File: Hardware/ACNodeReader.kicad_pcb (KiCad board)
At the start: 2 copper layers, 50 x 50 mm, 28 parts, among them J1 8P8C, J2 AVR-ISP-6, J3 Conn_01x04_Female, J5 Conn_01x04_Female, SW2 SW_Push, U1 L78L05_SOT89, U2 ATmega88PB-AU, U3 ISL8489EIBZ, U4 SI7060-B-00-IV, Y1 Crystal_GND24

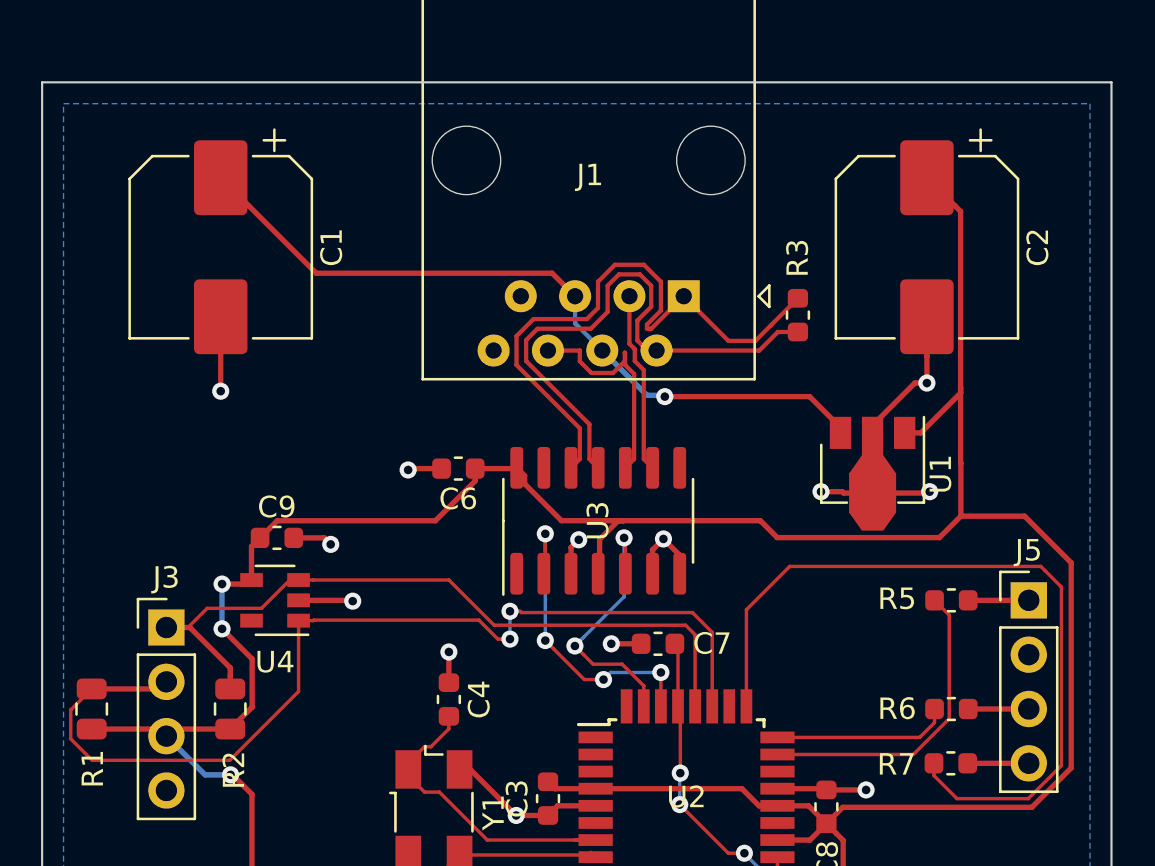
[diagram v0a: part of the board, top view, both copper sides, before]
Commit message: Toying with the circuit a bit
Removed the capacitor across reset since it breaks DebugWire which
is worth having usable because it helps when all hell breaks loose :-)

Added zero ohm links for switching LED from common anode to common cathode

Switched capacitors to (much smaller) MLCC variants in preparation for attempting
to cram everything into a smaller board
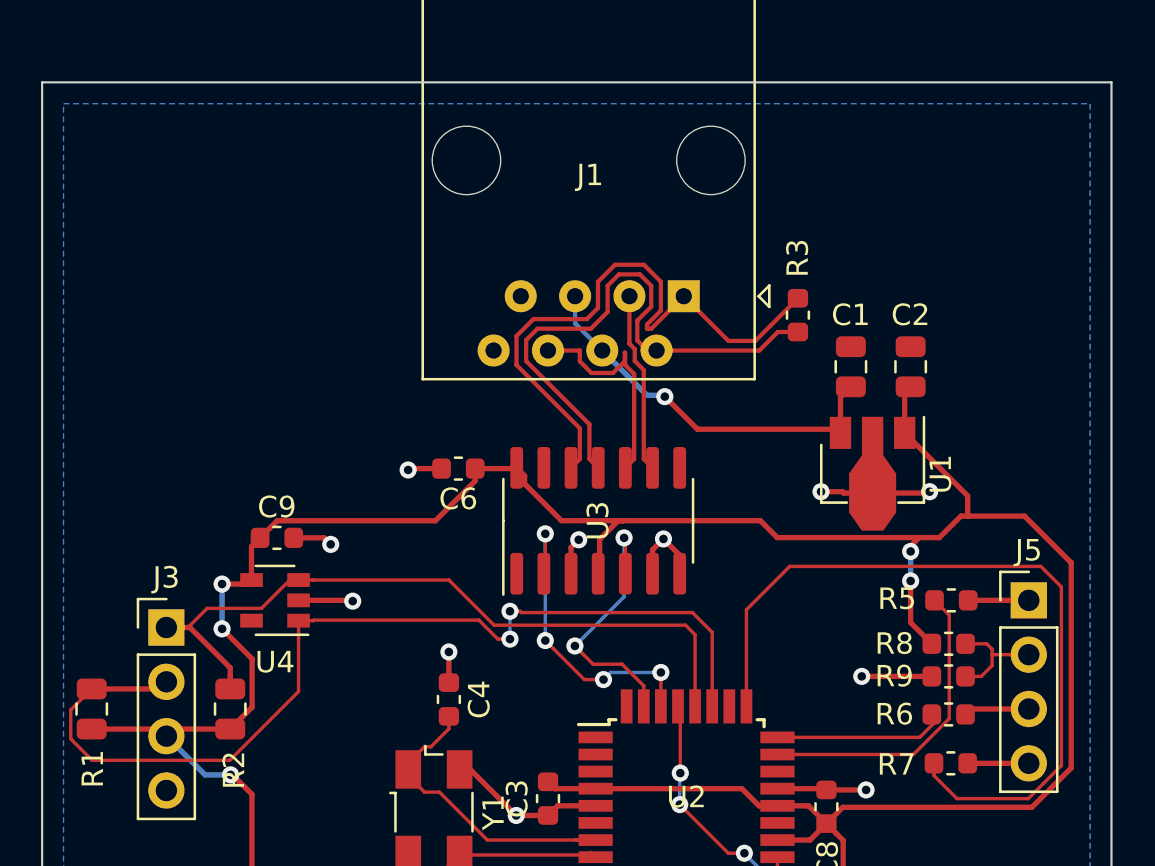
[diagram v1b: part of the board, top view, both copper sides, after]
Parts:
- removed C7: 4.7nF, Capacitor_SMD:C_0603_1608Metric
- added R8: DNF, Resistor_SMD:R_0603_1608Metric, F.Cu at (167.4, 111.3)
- added R9: 0R, Resistor_SMD:R_0603_1608Metric, F.Cu at (167.4, 112.8)
- C1, C2: value 470u -> 10u; footprint Capacitor_SMD:CP_Elec_8x10 -> Capacitor_SMD:C_0805_2012Metric
- moved C1 30.0 mm to (162.8, 98.3), turned to 90 degrees
- moved C2 5.64 mm to (165.6, 98.3), turned to 90 degrees
- moved R6 0.28 mm to (167.4, 114.6)
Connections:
- J5 pad 2: GND -> Net-(J5-Pad2)
- U2 pad 1: (no net) -> Net-(U2-Pad1)
- U2 pad 10: (no net) -> Net-(U2-Pad10)
- U2 pad 12: (no net) -> Net-(U2-Pad12)
- U2 pad 13: (no net) -> Net-(U2-Pad13)
- U2 pad 14: (no net) -> Net-(U2-Pad14)
- U2 pad 19: (no net) -> Net-(U2-Pad19)
- U2 pad 2: (no net) -> Net-(U2-Pad2)
- U2 pad 22: (no net) -> Net-(U2-Pad22)
- U2 pad 26: (no net) -> Net-(U2-Pad26)
- U2 pad 3: (no net) -> Net-(U2-Pad3)
- U2 pad 32: (no net) -> Net-(U2-Pad32)
- U2 pad 6: (no net) -> Net-(U2-Pad6)
- U2 pad 9: (no net) -> Net-(U2-Pad9)
- U4 pad 5: (no net) -> Net-(U4-Pad5)
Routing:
- net +12V: track 34.8 -> 18.4 mm
- net GND: track 55.6 -> 47.1 mm, vias 15 -> 13
- net +5V: track 155.4 -> 148.7 mm, vias 3 -> 5
- net Net-(J5-Pad2): track 0.00 -> 5.28 mm
- net Net-(J2-Pad5): track 24.6 -> 21.6 mm

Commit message: New, smaller, better PCB design
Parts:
- removed SW2: SW_Push, Button_Switch_THT:SW_PUSH_6mm
- added D1: D_Zener, Diode_SMD:D_SOD-323F, F.Cu at (116.6, 98.7)
- added H1: MountingHole, MountingHole:MountingHole_3.2mm_M3_DIN965, F.Cu at (117.5, 67.5)
- added H2: MountingHole, MountingHole:MountingHole_3.2mm_M3_DIN965, F.Cu at (142.8, 95.2)
- added J4: Conn_01x02_Male, Connector_PinHeader_2.54mm:PinHeader_1x02_P2.54mm_Horizontal, F.Cu at (145.7, 86.4)
- added J6: Conn_01x04_Male, Connector_PinHeader_2.54mm:PinHeader_1x04_P2.54mm_Horizontal, B.Cu at (114.1, 77.6)
- added J7: Conn_01x04_Male, Connector_PinHeader_2.54mm:PinHeader_1x04_P2.54mm_Vertical, F.Cu at (112.5, 66.0)
- J1: value 8P8C -> Conn_01x08_Male; footprint Connector_RJ:RJ45_Amphenol_54602-x08_Horizontal -> Connector_PinHeader_2.54mm:PinHeader_1x08_P2.54mm_Horizontal
- J2: footprint Tag-Connect:TC2030-MCP -> Tag-Connect:TC2030-MCP-NL
- J5: footprint Connector_PinHeader_2.54mm:PinHeader_1x04_P2.54mm_Vertical -> Connector_PinHeader_2.54mm:PinHeader_1x04_P2.54mm_Horizontal
- R1, R2, R4: footprint Resistor_SMD:R_0805_2012Metric -> Resistor_SMD:R_0603_1608Metric
- U4: value SI7060-B-00-IV -> LM75C; footprint Package_TO_SOT_SMD:SOT-23-5 -> Package_SO:SO-8_3.9x4.9mm_P1.27mm
- Y1: footprint Crystal:Crystal_SMD_Abracon_ABM3B-4Pin_5.0x3.2mm -> Crystal:Crystal_SMD_7050-4Pin_7.0x5.0mm
- moved R4 63.0 mm to (129.0, 72.8), turned to 0 degrees
- moved C8 53.8 mm to (123.8, 80.5), turned to 270 degrees
- moved C4 47.2 mm to (119.0, 73.8), turned to 180 degrees
- moved C5 46.7 mm to (119.2, 84.7), turned to 0 degrees
- moved J2 46.7 mm to (133.5, 91.1), turned to 0 degrees
- moved Y1 46.6 mm to (119.0, 79.3)
- moved R1 45.7 mm to (135.8, 69.4), turned to 0 degrees
- moved U2 45.4 mm to (130.2, 80.5)
- moved J3 44.1 mm to (134.1, 66.5), turned to 270 degrees
- moved R2 43.1 mm to (135.8, 71.2), turned to 0 degrees
- moved R9 43.0 mm to (142.2, 78.0)
- moved R3 42.7 mm to (118.5, 87.2), turned to 0 degrees
- moved R7 41.7 mm to (142.2, 83.6)
- moved C10 41.7 mm to (142.7, 87.4), turned to 270 degrees
- moved J5 41.7 mm to (145.7, 76.2)
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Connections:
- J1 pad 1: /RX+ -> GND
- J1 pad 2: /RX- -> GND
- J1 pad 3: /TX+ -> /TX-
- J1 pad 6: /TX- -> /TX+
- J1 pad 7: GND -> /RX-
- J1 pad 8: GND -> /RX+
- R1 pad 1: i2c_SDA -> i2c_SCL
- R2 pad 1: i2c_SCL -> i2c_SDA
- R5 pad 2: Net-(R5-Pad2) -> /LED1
- R6 pad 2: Net-(R6-Pad2) -> /LED2
- R7 pad 2: Net-(R7-Pad2) -> /LED3
- R8 pad 2: +5V -> GND
- R9 pad 1: GND -> +5V
- U2 pad 10: Net-(U2-Pad10) -> /LED2
- U2 pad 13: Net-(U2-Pad13) -> /LED3
- U2 pad 23: Net-(R5-Pad2) -> Net-(U2-Pad23)
- U2 pad 24: Net-(R6-Pad2) -> Net-(U2-Pad24)
- U2 pad 25: Net-(R7-Pad2) -> Net-(U2-Pad25)
- U2 pad 9: Net-(U2-Pad9) -> /LED1
- U4 pad 2: GND -> i2c_SCL
- U4 pad 3: i2c_SCL -> Net-(U4-Pad3)
- U4 pad 4: +5V -> GND
- U4 pad 5: Net-(U4-Pad5) -> GND
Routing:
- net Net-(R7-Pad2): track 36.5 -> 0.00 mm
- net /uC_TX: track 12.7 -> 42.0 mm
- net /uC_RX: track 14.8 -> 33.7 mm, vias 4 -> 2
- net /LED1: track 0.00 -> 18.7 mm
- net +5V: track 148.7 -> 166.2 mm, vias 5 -> 12
- net /LED2: track 0.00 -> 16.8 mm, vias 0 -> 2
- net GND: track 47.1 -> 62.4 mm, vias 13 -> 12
- net /RX+: track 28.6 -> 13.7 mm
- net Net-(R5-Pad2): track 14.5 -> 0.00 mm
- net /LED3: track 0.00 -> 12.9 mm, vias 0 -> 2
- net /RX-: track 26.5 -> 14.6 mm
- net i2c_SCL: track 34.8 -> 44.2 mm, vias 0 -> 1
- net Net-(C10-Pad1): track 30.3 -> 21.2 mm, vias 0 -> 2
- net Net-(R6-Pad2): track 8.27 -> 0.00 mm
- net Net-(J2-Pad1): track 17.7 -> 9.89 mm
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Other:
- board size 50 x 50 mm -> 40.4 x 42.7 mm
- copper layers 2 -> 4
- net class Power: trace_width 0.25 -> 0.5
- board text added: "+5V"
- board text added: "2020-08-27"
- board text added: "ACNode Reader Board V1.0 Designed by Michael Cullen"
- board text added: "Blue"
- board text added: "Blue/White"
- board text added: "Brown"
- board text added: "Brown/White"
- board text added: "Common"
- board text added: "Display?"
- board text added: "Fit R8 for common anode Fit R9 for common cathode Fit both for exciting times (briefly)"
- board text added: "GND"
- board text added: "Gr/Wh"
- board text added: "Green"
- board text added: "LED"
- board text added: "O/W"
- board text added: "Orange"
- board text added: "PN532 Goes Here"
- board text added: "RX"
- board text added: "Red"
- board text added: "Switch"
- board text added: "TX"
- board text added: "To ACNode"
- board text added: "To ACNode (Alternative)"

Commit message: Added note about reversed pinout
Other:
- board text added: "Connector Labelled Backwards!"

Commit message: Added some notes to schematic and updated firmware with new board support
getting there!
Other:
- board text added: "U4 Label upside down!"

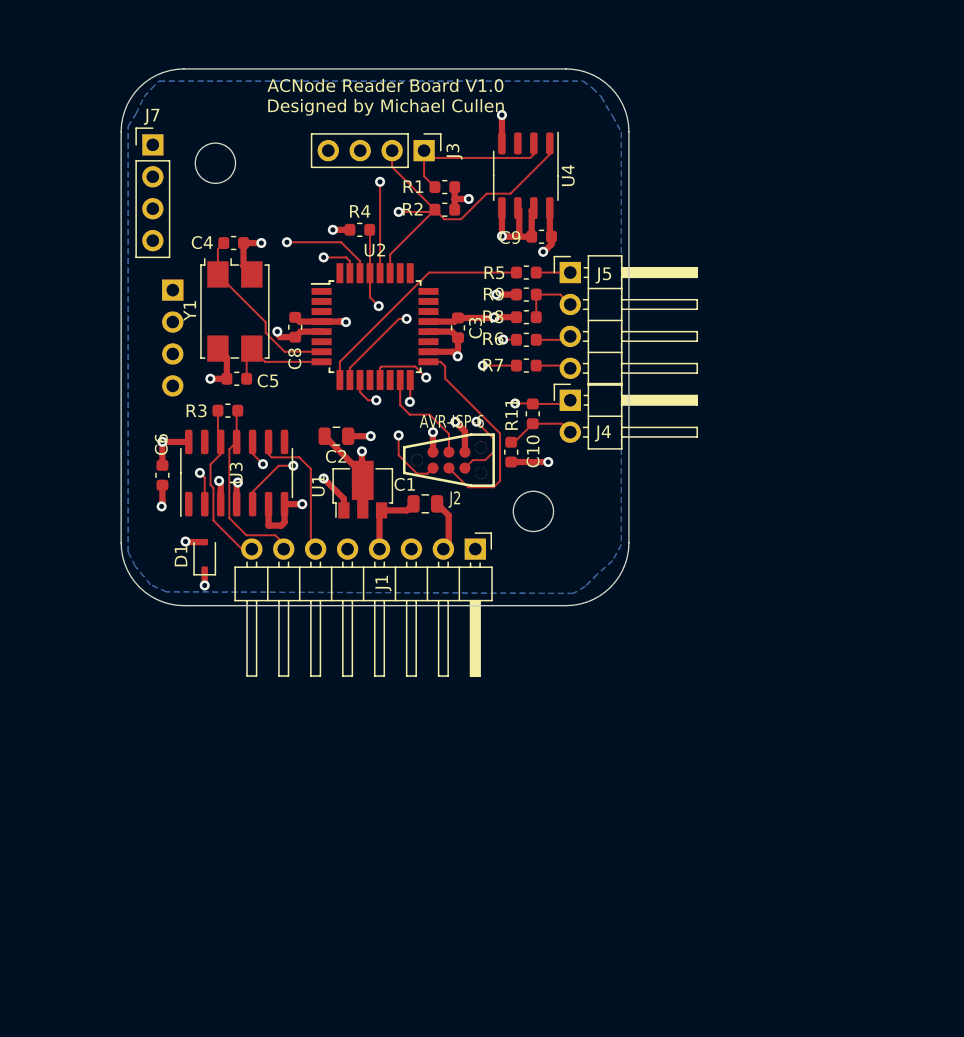
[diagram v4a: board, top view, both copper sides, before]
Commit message: Hardware V1.1 - 3.3V with chunkier 5V regulator
The 1.0 5V regulator wasn't chunky enough, so this board has a larger
one to support the current draw of the PN532 module. Additionally, a
capacitor has been added near to the PN532 module connector to assist in
smoothing the supply to it.

Most of the board now runs at 3.3V, derived from the 5V rail. This is to
support direct connection to an ACNode, which only support 3.3V IO. This
required slowing the AVR down to 12MHz. An alternative option would have
been to use a level shifter on the TX line.
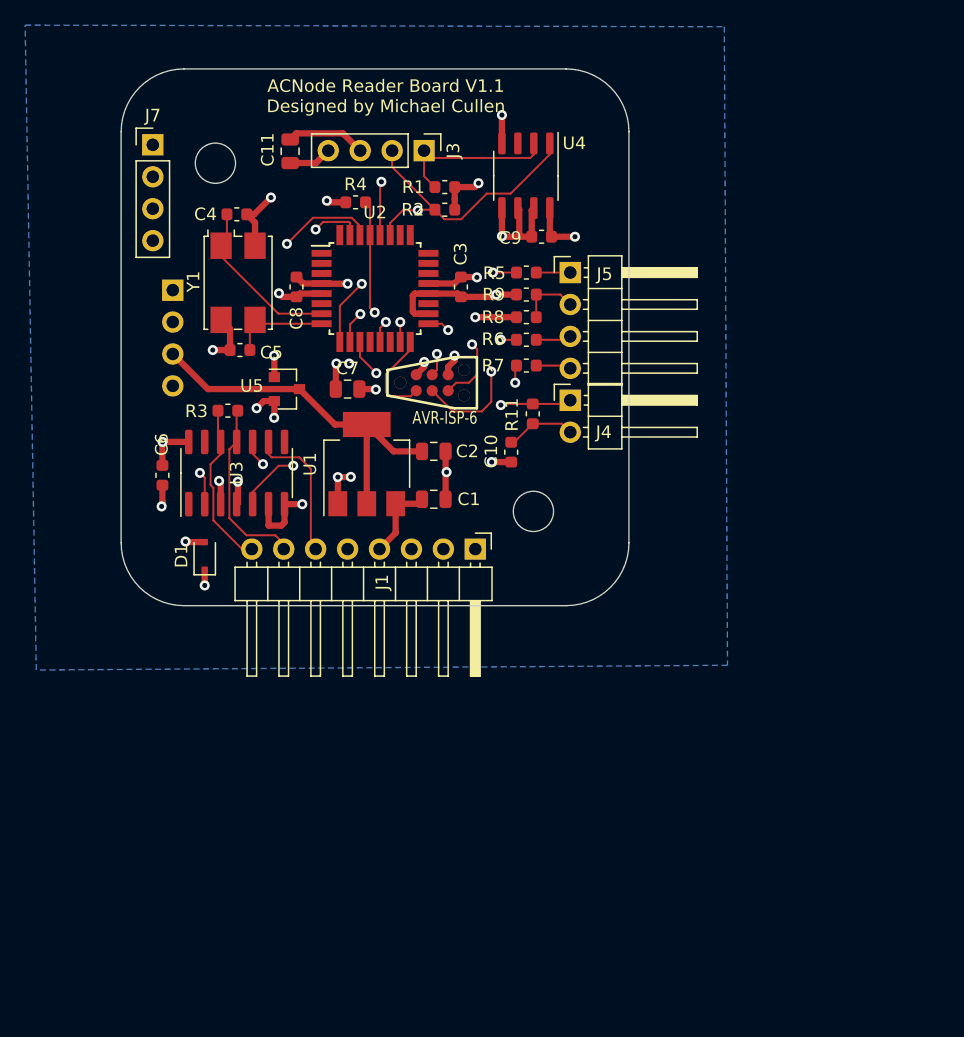
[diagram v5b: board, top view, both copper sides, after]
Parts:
- added C11: 10u, Capacitor_SMD:C_0805_2012Metric, F.Cu at (123.4, 66.5)
- added C7: 10u, Capacitor_SMD:C_0805_2012Metric, F.Cu at (128.0, 85.5)
- added U5: MCP1700-3302E_SOT23, Package_TO_SOT_SMD:SOT-23, F.Cu at (123.2, 85.5)
- U1: value L78L05_SOT89 -> NCP1117-5.0_SOT223; footprint Package_TO_SOT_SMD:SOT-89-3 -> Package_TO_SOT_SMD:SOT-223-3_TabPin2
- U3: value ISL8489EIBZ -> ISL3176EIBZ
- Y1: value Crystal_GND24 -> 12MHz
- moved C2 7.84 mm to (134.9, 90.4), turned to 0 degrees
- moved J2 6.30 mm to (132.2, 85.0)
- moved C3 3.27 mm to (137.0, 77.3)
- moved C8 3.21 mm to (124.0, 77.3)
- moved U2 3.03 mm to (130.2, 77.5)
- moved Y1 2.30 mm to (119.3, 77.0)
- moved C4 2.30 mm to (119.2, 71.6)
- moved C5 2.30 mm to (119.5, 82.4)
- moved R4 2.21 mm to (128.7, 70.6)
- moved U1 2.06 mm to (129.5, 91.4)
- moved C1 0.77 mm to (134.9, 94.2)
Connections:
- C3 pad 2: +5V -> +3V3
- C6 pad 1: +5V -> +3V3
- C8 pad 1: +5V -> +3V3
- C9 pad 1: +5V -> +3V3
- J2 pad 2: +5V -> +3V3
- R1 pad 2: +5V -> +3V3
- R11 pad 2: +5V -> +3V3
- R2 pad 2: +5V -> +3V3
- R4 pad 1: +5V -> +3V3
- R9 pad 1: +5V -> +3V3
- U1 pad 1: +5V -> GND
- U1 pad 2: GND -> +5V
- U2 pad 1: Net-(U2-Pad1) -> (no net)
- U2 pad 12: Net-(U2-Pad12) -> (no net)
- U2 pad 14: Net-(U2-Pad14) -> (no net)
- U2 pad 18: +5V -> +3V3
- U2 pad 19: Net-(U2-Pad19) -> (no net)
- U2 pad 2: Net-(U2-Pad2) -> (no net)
- U2 pad 20: +5V -> +3V3
- U2 pad 22: Net-(U2-Pad22) -> (no net)
- U2 pad 23: Net-(U2-Pad23) -> (no net)
- U2 pad 24: Net-(U2-Pad24) -> (no net)
- U2 pad 25: Net-(U2-Pad25) -> (no net)
- U2 pad 26: Net-(U2-Pad26) -> (no net)
- U2 pad 3: Net-(U2-Pad3) -> (no net)
- U2 pad 32: Net-(U2-Pad32) -> (no net)
- U2 pad 4: +5V -> +3V3
- U2 pad 6: Net-(U2-Pad6) -> (no net)
- U3 pad 14: +5V -> +3V3
- U3 pad 4: +5V -> +3V3
- U4 pad 3: Net-(U4-Pad3) -> (no net)
- U4 pad 8: +5V -> +3V3
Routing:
- net +3V3: track 0.00 -> 121.6 mm, vias 0 -> 13
- net +5V: track 166.2 -> 72.9 mm, vias 12 -> 0
- net GND: track 62.4 -> 58.2 mm, vias 12 -> 17
- net /LED3: track 12.9 -> 16.1 mm
- net i2c_SCL: track 44.2 -> 41.2 mm
- net i2c_SDA: track 48.6 -> 45.6 mm
- net Net-(J2-Pad3): track 17.3 -> 14.9 mm, vias 0 -> 2
- net Net-(J2-Pad1): track 9.89 -> 7.54 mm, vias 2 -> 0
- net /uC_RX: track 33.7 -> 35.8 mm
- net Net-(C10-Pad1): track 21.2 -> 19.7 mm
- net Net-(J2-Pad4): track 8.27 -> 7.37 mm, vias 0 -> 2
- net Net-(J2-Pad5): track 24.6 -> 23.7 mm
- net /uC_TX: track 42.0 -> 42.8 mm
- net Net-(C5-Pad2): track 8.56 -> 7.99 mm
- net Net-(C4-Pad2): track 14.0 -> 13.4 mm
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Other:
- board text added: "2020-09-22"
- board text added: "ACNode Reader Board V1.1 Designed by Michael Cullen"
- board text added: "Fit R8 for common cathode Fit R9 for common anode Fit both for exciting times (briefly)"
- board text removed: "2020-08-27"
- board text removed: "ACNode Reader Board V1.0 Designed by Michael Cullen"
- board text removed: "Connector Labelled Backwards!"
- board text removed: "Fit R8 for common anode Fit R9 for common cathode Fit both for exciting times (briefly)"
- board text removed: "U4 Label upside down!"

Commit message: Updated hardware with how I actually assembled it
I'm leaning towards the ATmega328PB, and also switched to 330R resistors on the LEDs
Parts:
- R5, R6, R7: value 1K -> 330R
- U2: value ATmega88PB-AU -> ATmega328PB-AU
